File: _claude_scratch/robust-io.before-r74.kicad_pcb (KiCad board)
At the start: 4 copper layers, 160 x 100 mm, 304 parts, among them J1 AVR-ISP-6, J10 Screw_Terminal_01x06, J14 Screw_Terminal_01x04, J15 Screw_Terminal_01x04, J16 Screw_Terminal_01x06, J18 Screw_Terminal_01x06, J19 Screw_Terminal_01x06, J20 UART, J3 Screw_Terminal_01x06, J4 Screw_Terminal_01x04, J5 Screw_Terminal_01x06, J6 Screw_Terminal_01x06, J9 Screw_Terminal_01x06, Q3 2N7002, Q4 2N7002, SW1 CHS-01TB, SW2 B3U-1000P, U1 DRV8876, U10 BTS7008, U11 BTS7008, U14 DRV8876, U2 ATmega1284P-A, U3 MCP2515, U4 TPS5604, U5 TPS5604, U6 MCP2562-E-MF, U7 MC33978, U8 BTS7008, U9 BTS7008, Y1 16MHz, Y2 12MHz

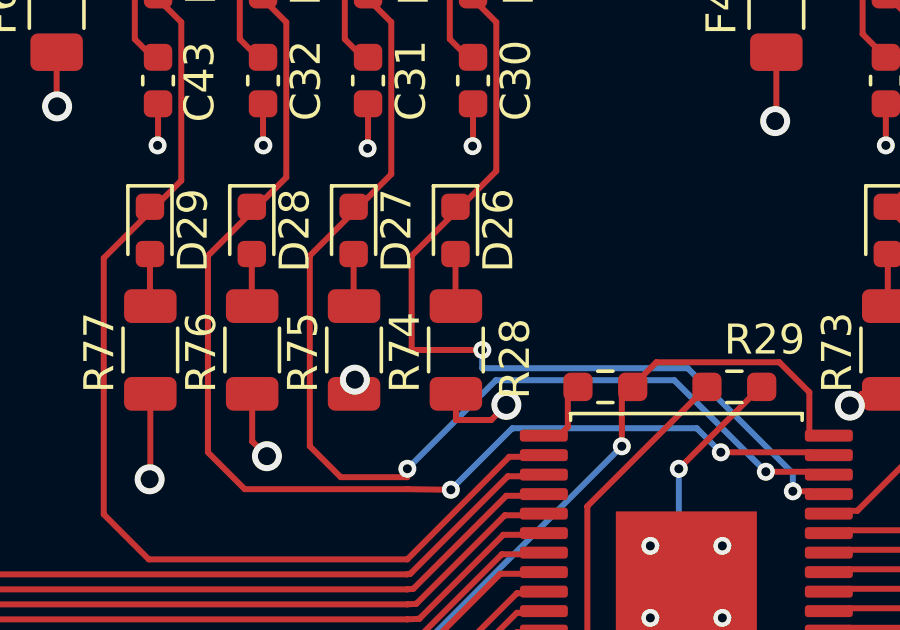
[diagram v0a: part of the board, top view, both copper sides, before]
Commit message: Rev A: release to fab (JLCPCB, 5 PCB / 2 assembled)
Board
- Outline set to exactly 160 x 100 mm; plane zones resized to match
- UART brought out on J20 (1x6 SMD, FTDI pinout) with series
  resistors R98/R99 and TVS D48
- J1 and J20 changed to SMD headers (C52016780, C41417363)
- L1/L2 moved to Sunlord SWPA4030S footprints; regulator tracks rerouted
- 41 test points added (35 top, 6 bottom), including SPI access
- Crystal case pins (Y1/Y2 pads 2, 4) tied to GND
- SW2 changed to 2-pin push button symbol
- R84-R91 changed from 2.2k to 10k to cut dissipation at 24 V
- Thermal vias in U1/U14 enlarged to 0.3 mm drill; 27 +24V vias added
  under U8-U11; solid plane connections on high-current pins
- Input/output rows and edge connectors aligned
- /inputs/_SG4 track and via moved clear of R74 pad 1

Schematic
- ERC cleared: no-connects, PWR_FLAGs, pin types, off-grid items
- Symbols moved to project library robust-io
- Test point symbols added on processor and power sheets

Rules
- Custom DRC rule for U7 pad-to-pad clearance (0.15 mm)
- Minimum through hole 0.2 mm; silk-to-edge check ignored

Fab outputs (fab/)
- make_gerbers.sh: Gerbers, drill and position export via kicad-cli
- JLC BOM with LCSC part numbers on all 50 SMD lines
- JLC placement file with per-part rotation offsets
  (cpl_rotation_offsets.json), verified in JLC placement preview
- Through-hole BOM and test point list

DRC: 4 library-mismatch warnings (J20, U1, U14, U7), 0 errors
ERC: clean
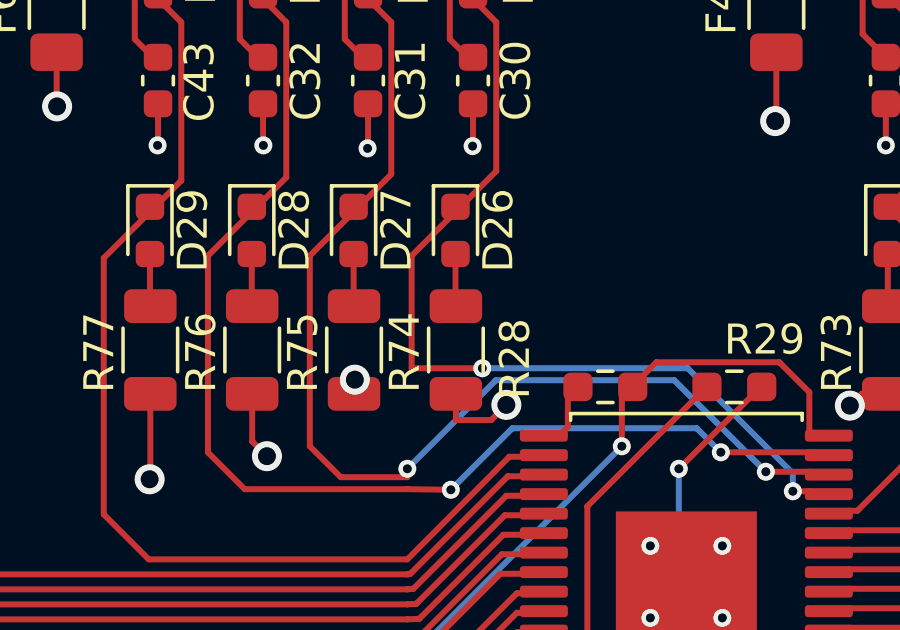
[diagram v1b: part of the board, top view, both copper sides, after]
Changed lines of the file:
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@@
 	)
 	(segment
-		(start 101.1436 52.07)
+		(start 101.1436 52.68)
 		(end 101.14357 48.92821)
 		(width 0.2)
@@
 	)
 	(segment
-		(start 103.5 52.07)
-		(end 101.1436 52.07)
+		(start 103.5 52.68)
+		(end 101.1436 52.68)
 		(width 0.2)
 		(layer "F.Cu")
@@
 	)
 	(via
-		(at 103.5 52.07)
+		(at 103.5 52.68)
 		(size 0.6)
 		(drill 0.3)
@@
 		(end 103.5 52.68)
 		(width 0.2)
-		(layer "B.Cu")
-		(net "/inputs/_SG4")
-	)
-	(segment
-		(start 103.5 52.07)
-		(end 103.5 52.68)
-		(width 0.2)
